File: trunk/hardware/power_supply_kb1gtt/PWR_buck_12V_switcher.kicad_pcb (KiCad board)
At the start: 2 copper layers, 38.1 x 38.7 mm, 19 parts, among them P1 CONN_2, P2 CONN_1, P3 CONN_2, Q1 MOS_PRO, U1 LM2596

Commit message: some updates
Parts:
- C2, C3: value 220uF -> 220uF 16V
- turned C2 to 180 degrees
- turned C3 to 180 degrees
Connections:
- C2 pad 1: GND -> /FB
- C2 pad 2: /FB -> GND
- C3 pad 1: GND -> /5V-REG
- C3 pad 2: /5V-REG -> GND
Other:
- board text added: "BAT GND"
- board text added: "R0.2"
- board text removed: "GND BAT"
- board text removed: "R0.1"
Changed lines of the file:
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@@
     (area 160.02 92.71 212.697787 141.986)
     (thickness 1.6002)
-    (drawings 16)
+    (drawings 18)
     (tracks 108)
     (zones 0)
@@
   (title_block
     (title "PWR buck 12V switcher regulator")
-    (rev "R 0.1")
+    (rev "R 0.2")
     (company http://code.google.com/p/daecu/)
   )
@@
     (18 B.Paste user)
     (19 F.Paste user)
-    (20 B.SilkS user hide)
+    (20 B.SilkS user)
     (21 F.SilkS user)
     (22 B.Mask user)
-    (23 F.Mask user hide)
+    (23 F.Mask user)
     (24 Dwgs.User user)
     (25 Cmts.User user)
@@
   (net 7 GND)
   (net 8 N-000001)
-  (net 9 N-000007)
+  (net 9 N-000008)
   (net_class Default "This is the default net class."
     (clearance 0.1778)
@@
     (add_net "")
     (add_net N-000001)
-    (add_net N-000007)
+    (add_net N-000008)
   )
   (net_class "10A EXT" ""
@@
   )
   (module SM2512 (layer Front-ext)
-    (at 186.69 109.22)
+    (at 186.69 109.22 180)
     (tags "CMS SM")
     (attr smd)
-    (fp_text reference C2 (at -0.8001 0 90) (layer F.SilkS)
+    (fp_text reference C2 (at -0.8001 0 270) (layer F.SilkS)
       (effects (font (size 0.889 0.762) (thickness 0.127)))
     )
-    (fp_text value 220uF (at 0.89916 0 90) (layer F.SilkS) hide
+    (fp_text value "220uF 16V" (at 0.89916 0 270) (layer F.SilkS) hide
       (effects (font (size 0.889 0.762) (thickness 0.127)))
     )
     (fp_line (start -3.99956 -2.10058) (end -3.99956 2.10058) (layer F.SilkS) (width 0.14986))
-    (fp_text user + (at -4.59994 2.30124) (layer F.SilkS)
+    (fp_text user + (at -4.59994 2.30124 180) (layer F.SilkS)
       (effects (font (size 0.7 0.7) (thickness 0.15)))
     )
@@
     (fp_line (start -1.99898 -2.10566) (end -4.28498 -2.10566) (layer F.SilkS) (width 0.14986))
     (fp_line (start -4.28244 2.10566) (end -1.99644 2.10566) (layer F.SilkS) (width 0.14986))
-    (pad 1 smd rect (at -2.99974 0) (size 1.99898 2.99974)
-      (layers Front-ext F.Paste F.Mask)
-      (net 7 GND)
-    )
-    (pad 2 smd rect (at 2.99974 0) (size 1.99898 2.99974)
+    (pad 1 smd rect (at -2.99974 0 180) (size 1.99898 2.99974)
       (layers Front-ext F.Paste F.Mask)
       (net 2 /FB)
     )
+    (pad 2 smd rect (at 2.99974 0 180) (size 1.99898 2.99974)
+      (layers Front-ext F.Paste F.Mask)
+      (net 7 GND)
+    )
     (model smd\chip_smd_pol_wide.wrl
       (at (xyz 0 0 0))
@@
   )
   (module SM2512 (layer Front-ext)
-    (at 196.215 109.22)
+    (at 196.215 109.22 180)
     (tags "CMS SM")
     (attr smd)
-    (fp_text reference C3 (at 0.635 0 90) (layer F.SilkS)
+    (fp_text reference C3 (at 0.635 0 270) (layer F.SilkS)
       (effects (font (size 0.889 0.762) (thickness 0.127)))
     )
-    (fp_text value 220uF (at 0.89916 0 90) (layer F.SilkS) hide
+    (fp_text value "220uF 16V" (at 0.89916 0 270) (layer F.SilkS) hide
       (effects (font (size 0.889 0.762) (thickness 0.127)))
     )
     (fp_line (start -3.99956 -2.10058) (end -3.99956 2.10058) (layer F.SilkS) (width 0.14986))
-    (fp_text user + (at -4.59994 2.30124) (layer F.SilkS)
+    (fp_text user + (at -4.59994 2.30124 180) (layer F.SilkS)
       (effects (font (size 0.7 0.7) (thickness 0.15)))
     )
@@
     (fp_line (start -1.99898 -2.10566) (end -4.28498 -2.10566) (layer F.SilkS) (width 0.14986))
     (fp_line (start -4.28244 2.10566) (end -1.99644 2.10566) (layer F.SilkS) (width 0.14986))
-    (pad 1 smd rect (at -2.99974 0) (size 1.99898 2.99974)
-      (layers Front-ext F.Paste F.Mask)
-      (net 7 GND)
-    )
-    (pad 2 smd rect (at 2.99974 0) (size 1.99898 2.99974)
+    (pad 1 smd rect (at -2.99974 0 180) (size 1.99898 2.99974)
       (layers Front-ext F.Paste F.Mask)
       (net 1 /5V-REG)
+    )
+    (pad 2 smd rect (at 2.99974 0 180) (size 1.99898 2.99974)
+      (layers Front-ext F.Paste F.Mask)
+      (net 7 GND)
     )
     (model smd\chip_smd_pol_wide.wrl
@@
     (pad 2 smd rect (at 0.9525 0) (size 0.889 1.397)
       (layers Front-ext F.Paste F.Mask)
-      (net 9 N-000007)
+      (net 9 N-000008)
     )
     (model smd/chip_cms.wrl
@@
     (pad 1 smd rect (at -1.04902 0) (size 1.19888 1.19888)
       (layers Front-ext F.Paste F.Mask)
-      (net 9 N-000007)
+      (net 9 N-000008)
     )
     (pad 2 smd rect (at 1.04902 0) (size 1.19888 1.19888)
@@
     (tags CONNECTOR)
     (attr virtual)
-    (fp_text reference P3 (at 3.175 7.62 360) (layer F.SilkS)
+    (fp_text reference P3 (at 3.175 8.255 360) (layer F.SilkS)
       (effects (font (size 1.778 1.778) (thickness 0.127)))
     )
@@
     )
   )
+  (gr_line (start 190.881 106.807) (end 190.881 111.633) (angle 90) (layer F.SilkS) (width 0.254))
+  (gr_line (start 200.406 106.68) (end 200.406 111.633) (angle 90) (layer F.SilkS) (width 0.254))
   (dimension 38.1 (width 0.381) (layer Cmts.User)
     (gr_text "1.5000 in" (at 181.61 140.207999) (layer Cmts.User)
@@
   (gr_line (start 162.56 125.095) (end 162.56 133.985) (angle 90) (layer Edge.Cuts) (width 0.254))
   (gr_line (start 200.66 125.095) (end 200.66 133.985) (angle 90) (layer Edge.Cuts) (width 0.254))
-  (gr_text "GND\n\n5V" (at 196.85 101.6) (layer B.SilkS)
+  (gr_text "GND\n\n\n5V" (at 189.865 127.635) (layer B.SilkS)
     (effects (font (size 0.889 0.889) (thickness 0.127)) (justify mirror))
   )
-  (gr_text "GND\n\nBAT" (at 167.64 120.65) (layer B.SilkS)
+  (gr_text "BAT\n\n\nGND" (at 172.72 127.635) (layer B.SilkS)
     (effects (font (size 0.889 0.889) (thickness 0.127)) (justify mirror))
   )
@@
     (effects (font (size 1.016 1.016) (thickness 0.127)) (justify left mirror))
   )
-  (gr_text R0.1 (at 168.275 102.235) (layer B.SilkS)
+  (gr_text R0.2 (at 168.275 102.235) (layer B.SilkS)
     (effects (font (size 1.016 1.016) (thickness 0.127)) (justify mirror))
   )
-  (gr_text P3 (at 199.39 99.695) (layer B.SilkS)
+  (gr_text P3 (at 197.485 129.54) (layer B.SilkS)
     (effects (font (size 1.016 1.016) (thickness 0.127)) (justify mirror))
   )
@@
     (effects (font (size 1.016 1.016) (thickness 0.127)) (justify mirror))
   )
-  (gr_text P1 (at 164.465 118.11) (layer B.SilkS)
+  (gr_text P1 (at 165.1 130.175) (layer B.SilkS)
     (effects (font (size 1.016 1.016) (thickness 0.127)) (justify mirror))
   )

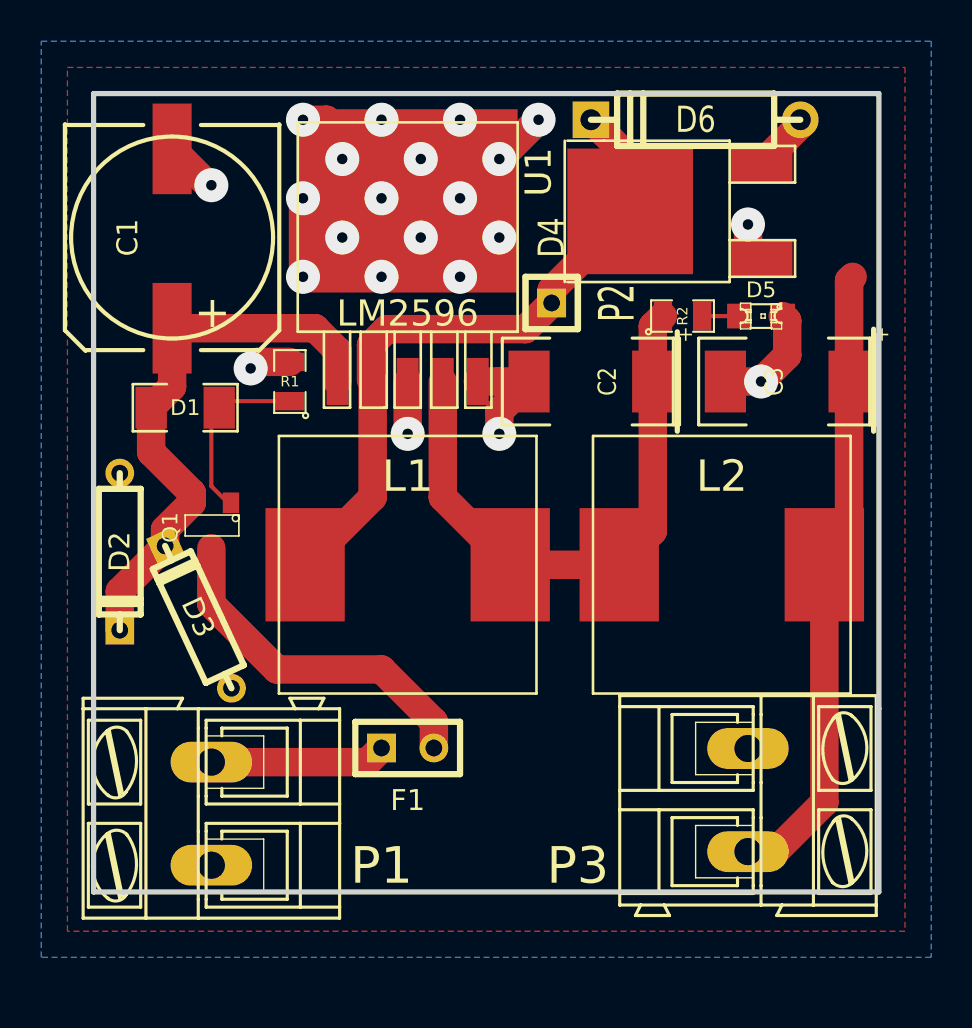
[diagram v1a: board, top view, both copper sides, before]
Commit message: renaming to 130 range
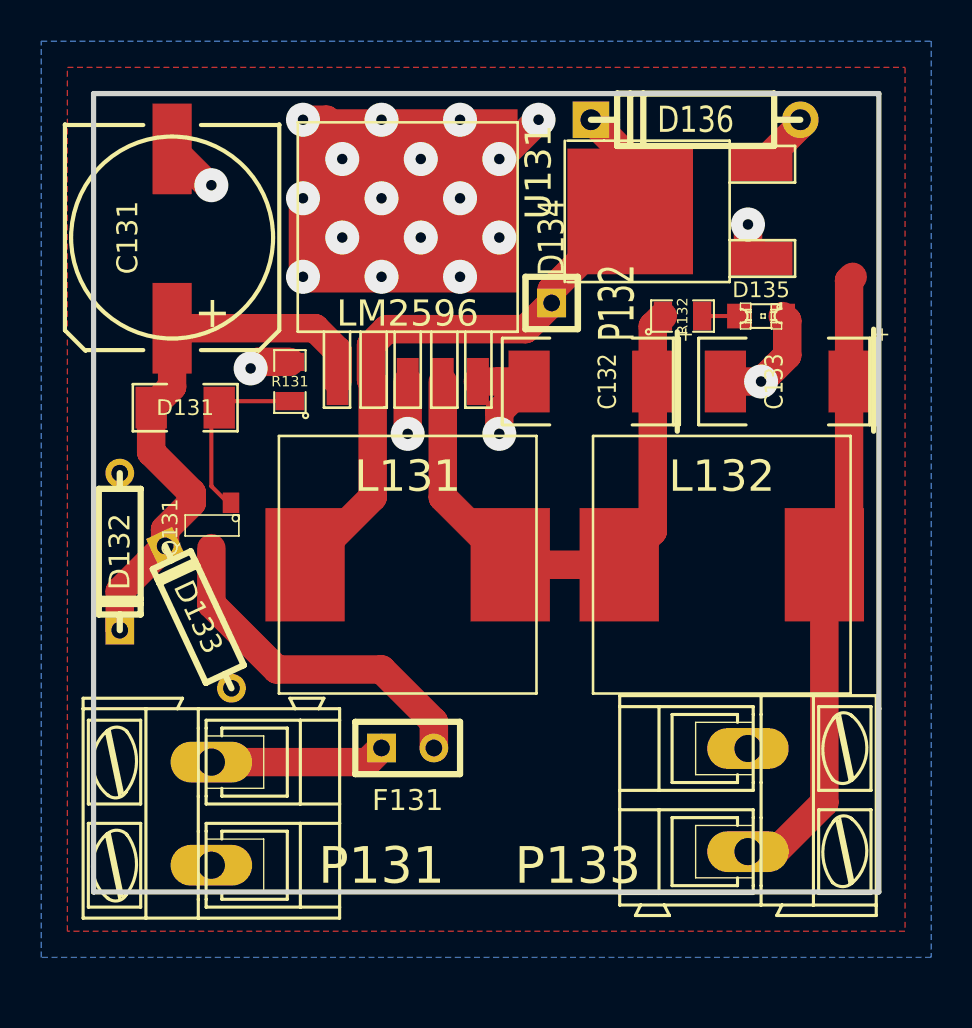
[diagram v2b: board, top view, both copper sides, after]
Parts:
- D132: renamed from D2; footprint D3 -> D133
- D133: renamed from D3; footprint D3 -> D133
- D136: renamed from D6; footprint D4 -> D134
- renumbered C1 to C131, C2 to C132, C3 to C133, D1 to D131, D4 to D134, D5 to D135, F1 to F131, L1 to L131, L2 to L132, P1 to P131, P2 to P132, P3 to P133, Q1 to Q131, R1 to R131, R2 to R132, U1 to U131
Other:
- board text added: "P131"
- board text added: "P133"
- board text removed: "P1"
- board text removed: "P3"
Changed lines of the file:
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@@
     (tags "CMS SM")
     (attr smd)
-    (fp_text reference C2 (at -0.8001 0 270) (layer F.SilkS)
+    (fp_text reference C132 (at -0.8001 0 270) (layer F.SilkS)
       (effects (font (size 0.889 0.762) (thickness 0.127)))
     )
@@
     (tags "CMS SM")
     (attr smd)
-    (fp_text reference C3 (at 0.635 0 270) (layer F.SilkS)
+    (fp_text reference C133 (at 0.635 0 270) (layer F.SilkS)
       (effects (font (size 0.889 0.762) (thickness 0.127)))
     )
@@
   (module SM100uH (layer Front-ext)
     (at 177.8 118.11)
-    (fp_text reference L1 (at 0 -4.2926) (layer F.SilkS)
+    (fp_text reference L131 (at 0 -4.2926) (layer F.SilkS)
       (effects (font (size 1.524 1.524) (thickness 0.3048)))
     )
@@
   (module SM100uH (layer Front-ext)
     (at 193.04 118.11)
-    (fp_text reference L2 (at 0 -4.2926) (layer F.SilkS)
+    (fp_text reference L132 (at 0 -4.2926) (layer F.SilkS)
       (effects (font (size 1.524 1.524) (thickness 0.3048)))
     )
@@
     (at 191.135 106.045)
     (attr smd)
-    (fp_text reference R2 (at 0 0 90) (layer F.SilkS)
+    (fp_text reference R132 (at 0 0 90) (layer F.SilkS)
       (effects (font (size 0.508 0.508) (thickness 0.127)))
     )
@@
     (tags "LED 0805 SMD")
     (attr smd)
-    (fp_text reference D5 (at 0 -1.27) (layer F.SilkS)
+    (fp_text reference D135 (at 0 -1.27) (layer F.SilkS)
       (effects (font (size 0.762 0.762) (thickness 0.127)))
     )
@@
     (at 177.8 109.22)
     (tags "CMS DPACK")
-    (fp_text reference U1 (at 6.35 -10.16 90) (layer F.SilkS)
+    (fp_text reference U131 (at 6.35 -10.16 90) (layer F.SilkS)
       (effects (font (size 1.27 1.27) (thickness 0.1524)))
     )
@@
     (tags "CMD DPACK")
     (attr smd)
-    (fp_text reference D4 (at -1.27 -10.16 90) (layer F.SilkS)
+    (fp_text reference D134 (at -1.27 -10.16 90) (layer F.SilkS)
       (effects (font (size 1.27 1.016) (thickness 0.127)))
     )
@@
     (at 166.37 102.235 90)
     (attr smd)
-    (fp_text reference C1 (at 0 -2.159 90) (layer F.SilkS)
+    (fp_text reference C131 (at 0 -2.159 90) (layer F.SilkS)
       (effects (font (size 1.016 1.00076) (thickness 0.15748)))
     )
@@
     (at 172.085 109.22 90)
     (attr smd)
-    (fp_text reference R1 (at 0 0 180) (layer F.SilkS)
+    (fp_text reference R131 (at 0 0 180) (layer F.SilkS)
       (effects (font (size 0.508 0.508) (thickness 0.127)))
     )
@@
     (descr "Connecteurs 1 pin")
     (tags "CONN DEV")
-    (fp_text reference P2 (at 0 3.175 90) (layer F.SilkS)
+    (fp_text reference P132 (at 0 3.175 90) (layer F.SilkS)
       (effects (font (size 1.72974 1.08712) (thickness 0.27178)))
     )
@@
     (at 167.005 110.49 180)
     (attr smd)
-    (fp_text reference D1 (at 0 0 180) (layer F.SilkS)
+    (fp_text reference D131 (at 0 0 180) (layer F.SilkS)
       (effects (font (size 0.762 0.762) (thickness 0.127)))
     )
@@
     (at 168.275 116.205 180)
     (tags SOT23)
-    (fp_text reference Q1 (at 1.99898 -0.09906 270) (layer F.SilkS)
+    (fp_text reference Q131 (at 1.99898 -0.09906 270) (layer F.SilkS)
       (effects (font (size 0.762 0.762) (thickness 0.11938)))
     )
@@
     )
   )
-  (module D4 (layer Front-ext)
+  (module D134 (layer Front-ext)
     (at 191.77 96.52 180)
     (descr "Diode 4 pas")
     (tags "DIODE DEV")
-    (fp_text reference D6 (at 0 0 180) (layer F.SilkS)
+    (fp_text reference D136 (at 0 0 180) (layer F.SilkS)
       (effects (font (size 1.27 1.016) (thickness 0.2032)))
     )
@@
     (tags CONNECTOR)
     (attr virtual)
-    (fp_text reference P1 (at -2.54 8.255 180) (layer F.SilkS)
+    (fp_text reference P131 (at -2.54 8.255 180) (layer F.SilkS)
       (effects (font (size 1.778 1.778) (thickness 0.127)))
     )
@@
     (tags CONNECTOR)
     (attr virtual)
-    (fp_text reference P3 (at 3.175 8.255 360) (layer F.SilkS)
+    (fp_text reference P133 (at 3.175 8.255 360) (layer F.SilkS)
       (effects (font (size 1.778 1.778) (thickness 0.127)))
     )
@@
     )
   )
-  (module D3 (layer Front-ext)
+  (module D133 (layer Front-ext)
     (at 167.64 120.65 115)
     (descr "Diode 3 pas")
     (tags "DIODE DEV")
-    (fp_text reference D3 (at 0 0 115) (layer F.SilkS)
+    (fp_text reference D133 (at 0 0 115) (layer F.SilkS)
       (effects (font (size 1.016 1.016) (thickness 0.2032)))
     )
@@
     )
   )
-  (module D3 (layer Front-ext)
+  (module D133 (layer Front-ext)
     (at 163.83 117.475 270)
     (descr "Diode 3 pas")
     (tags "DIODE DEV")
-    (fp_text reference D2 (at 0 0 270) (layer F.SilkS)
+    (fp_text reference D132 (at 0 0 270) (layer F.SilkS)
       (effects (font (size 1.016 1.016) (thickness 0.2032)))
     )
@@
     (descr "Connecteurs 2 pins")
     (tags "CONN DEV")
-    (fp_text reference F1 (at 0 2.54) (layer F.SilkS)
+    (fp_text reference F131 (at 0 2.54) (layer F.SilkS)
       (effects (font (size 1.016 1.016) (thickness 0.127)))
     )
@@
     (effects (font (size 1.016 1.016) (thickness 0.127)) (justify mirror))
   )
-  (gr_text P3 (at 197.485 129.54) (layer B.SilkS)
+  (gr_text P133 (at 197.485 129.54) (layer B.SilkS)
     (effects (font (size 1.016 1.016) (thickness 0.127)) (justify mirror))
   )
@@
     (effects (font (size 1.016 1.016) (thickness 0.127)) (justify mirror))
   )
-  (gr_text P1 (at 165.1 130.175) (layer B.SilkS)
+  (gr_text P131 (at 165.1 130.175) (layer B.SilkS)
     (effects (font (size 1.016 1.016) (thickness 0.127)) (justify mirror))
   )

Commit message: better net name
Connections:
- net /5V-REG renamed /5V
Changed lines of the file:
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@@
   )
   (net 0 "")
-  (net 1 /5V-REG)
+  (net 1 /5V)
   (net 2 /FB)
   (net 3 /OUT)
@@
     (uvia_drill 0.254)
     (add_net "")
+    (add_net /5V)
     (add_net N-000001)
     (add_net N-000008)
@@
     (uvia_dia 0.762)
     (uvia_drill 0.254)
-    (add_net /5V-REG)
     (add_net /FB)
     (add_net /OUT)
@@
     (pad 1 smd rect (at -2.99974 0 180) (size 1.99898 2.99974)
       (layers F.Cu F.Paste F.Mask)
-      (net 1 /5V-REG)
+      (net 1 /5V)
     )
     (pad 2 smd rect (at 2.99974 0 180) (size 1.99898 2.99974)
@@
     (pad 2 smd rect (at 4.97586 0) (size 3.85064 5.4991)
       (layers F.Cu F.Paste F.Mask)
-      (net 1 /5V-REG)
+      (net 1 /5V)
     )
     (model smd/self_cms_we-pd3.wrl
@@
     (pad 2 thru_hole oval (at 2.4892 0 270) (size 1.9812 3.9624) (drill 1.3208)
       (layers *.Cu F.Paste F.SilkS F.Mask)
-      (net 1 /5V-REG)
-    )
-  )
+      (net 1 /5V)
+    )
+  )

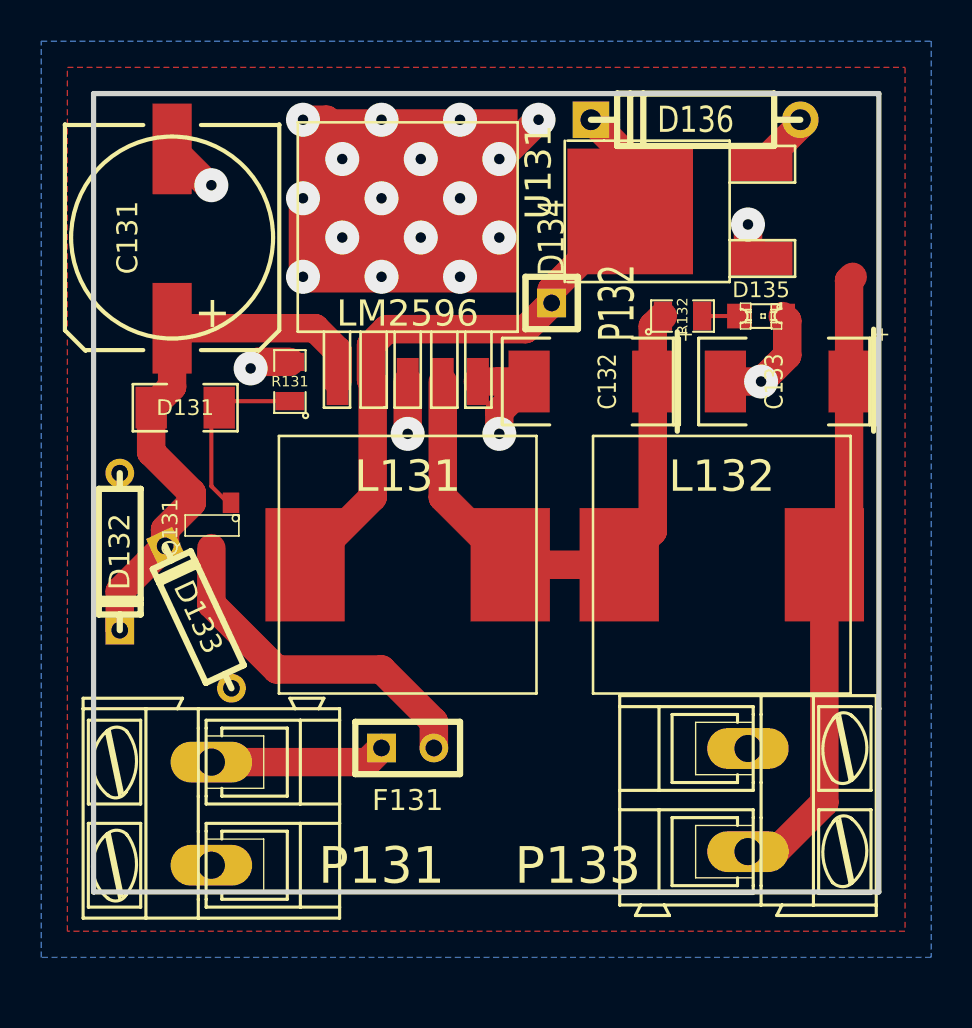
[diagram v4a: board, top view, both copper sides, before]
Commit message: 
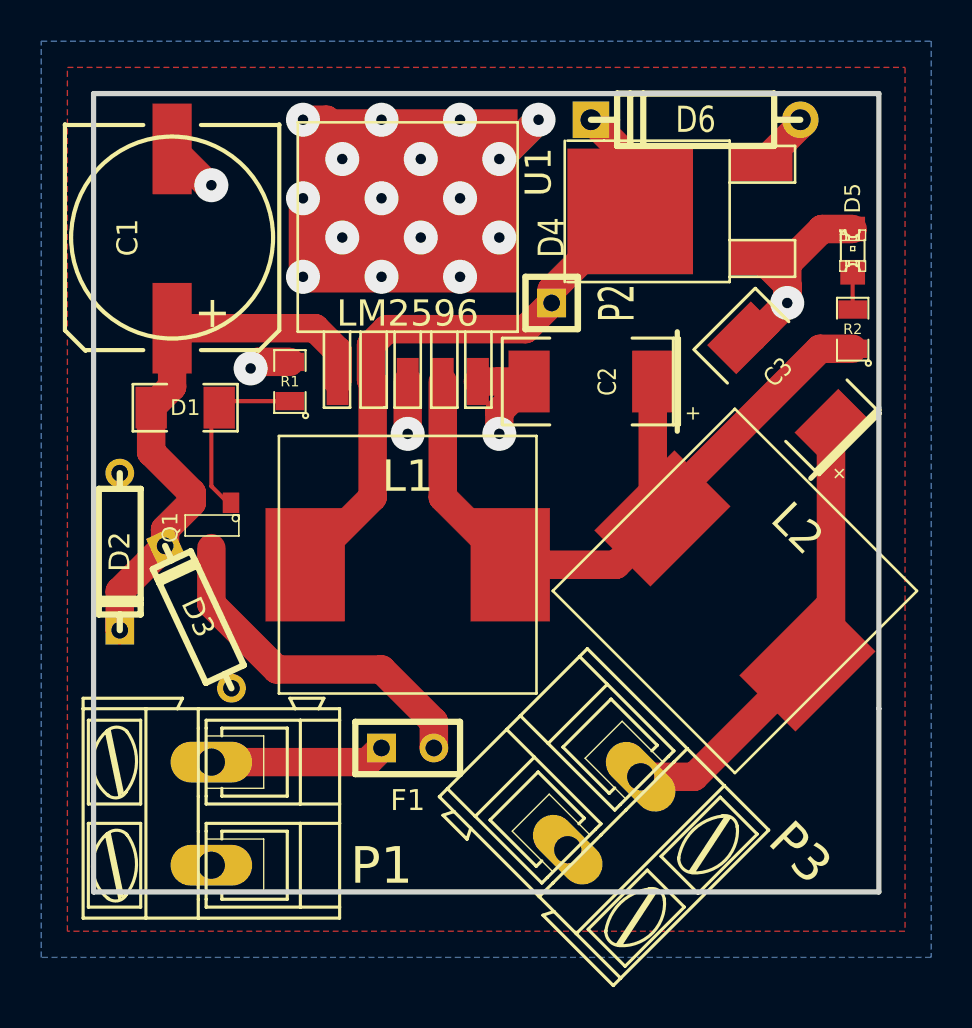
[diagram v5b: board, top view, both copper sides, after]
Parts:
- removed C132: 220uF 16V, SM2512
- added C2: 220uF 16V, SM2512, F.Cu at (186.7, 109.2)
- D2: renamed from D132; footprint D133 -> D3
- D3: renamed from D133; footprint D133 -> D3
- D6: renamed from D136; footprint D134 -> D4
- moved R2 8.28 mm to (199.4, 106.7), turned to 90 degrees
- moved P3 7.01 mm to (187.3, 130.2), turned to 225 degrees
- moved D5 5.46 mm to (199.4, 102.9), turned to 90 degrees
- moved L2 1.42 mm to (193.7, 119.4), turned to 315 degrees
- turned C3 to 135 degrees
- renumbered C131 to C1, C133 to C3, D131 to D1, D134 to D4, D135 to D5, F131 to F1, L131 to L1, L132 to L2, P131 to P1, P132 to P2, P133 to P3, Q131 to Q1, R131 to R1, R132 to R2, U131 to U1
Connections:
- C3 pad 1: /5V -> /5V-REG
- L2 pad 2: /5V -> /5V-REG
- P3 pad 1: GND -> /5V-REG
- P3 pad 2: /5V -> GND
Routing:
- net /5V: track 30.8 -> 0.00 mm
- net /5V-REG: track 0.00 -> 22.4 mm
- net /FB: track 28.5 -> 38.4 mm
- net GND: track 79.2 -> 83.0 mm, vias 22 -> 21
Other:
- board text added: "5V GND"
- board text added: "P1"
- board text added: "P3"
- board text added: "R0.3"
- board text removed: "GND 5V"
- board text removed: "P131"
- board text removed: "P133"
- board text removed: "R0.2"
